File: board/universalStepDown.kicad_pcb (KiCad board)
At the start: 4 copper layers, 19.5 x 10.5 mm, 15 parts, among them J1 IO, U1 SY8105

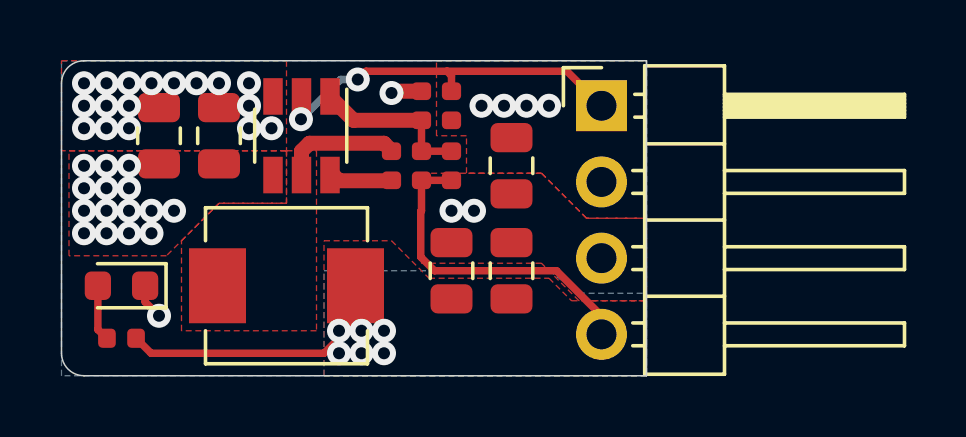
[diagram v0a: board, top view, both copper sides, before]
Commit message: Fix issues by cednik, prepare multi-voltage variant
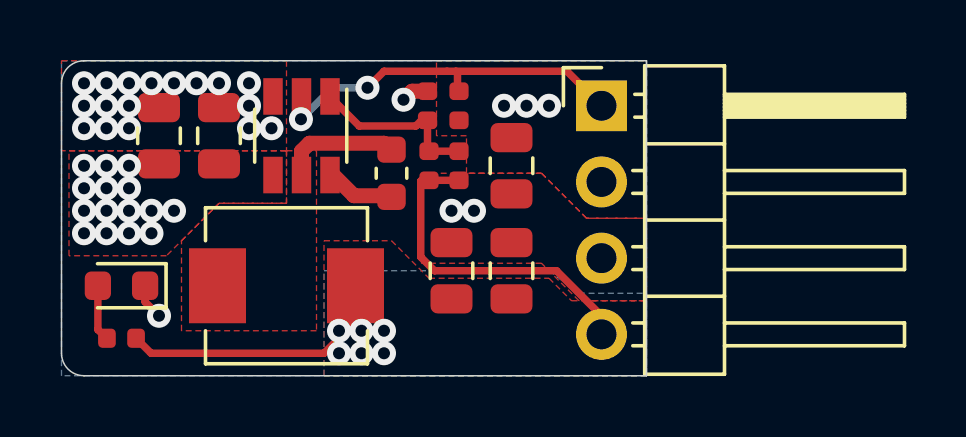
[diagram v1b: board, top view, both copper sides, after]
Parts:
- C2: footprint Capacitor_SMD:C_0402_1005Metric -> Capacitor_SMD:C_0603_1608Metric
- R2: value 27k -> 27k (for 5V)/44.2k (for 3V3)
- R3: value 47k -> 1M
- moved C2 0.25 mm to (86.0, 85.2)
- moved C3 0.25 mm to (88.2, 85.0)
- moved R1 0.25 mm to (87.2, 85.0)
- moved R3 0.25 mm to (88.2, 83.0)
- moved R2 0.20 mm to (87.2, 83.0)
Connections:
- net +5V renamed VOUT
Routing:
- net VCC: vias 19 -> 18
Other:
- board text added: "${VOLTAGE}"
- board text added: "EN VIN GND VOUT"
- board text removed: "EN VIN GND 5VOUT"

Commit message: Prepare Makefile
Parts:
- J1: footprint Connector_PinHeader_2.54mm:PinHeader_1x04_P2.54mm_Horizontal -> universalStepDown:PinHeader_1x04_P2.54mm_Horizontal
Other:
- board text added: "VOLTAGE_VARIANT"
- board text removed: "${VOLTAGE}"
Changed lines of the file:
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@@
     (add_net VOUT)
+  )
+  (module universalStepDown:PinHeader_1x04_P2.54mm_Horizontal (layer F.Cu)
+    (at 93 83)
+    (descr "Through hole angled pin header, 1x04, 2.54mm pitch, 6mm pin length, single row")
+    (tags "Through hole angled pin header THT 1x04 2.54mm single row")
+    (fp_text reference J1 (at 0 -2.5) (layer F.SilkS) hide
+      (effects (font (size 1 1) (thickness 0.15)))
+    )
+    (fp_text value IO (at 0 10.5) (layer F.Fab)
+      (effects (font (size 1 1) (thickness 0.15)))
+    )
+    (fp_line (start -0.32 -0.32) (end 1.5 -0.32) (layer F.Fab) (width 0.1))
+    (fp_line (start -0.32 -0.32) (end -0.32 0.32) (layer F.Fab) (width 0.1))
+    (fp_line (start -0.32 0.32) (end 1.5 0.32) (layer F.Fab) (width 0.1))
+    (fp_line (start -0.32 2.22) (end 1.5 2.22) (layer F.Fab) (width 0.1))
+    (fp_line (start -0.32 2.22) (end -0.32 2.86) (layer F.Fab) (width 0.1))
+    (fp_line (start -0.32 2.86) (end 1.5 2.86) (layer F.Fab) (width 0.1))
+    (fp_line (start -0.32 4.76) (end 1.5 4.76) (layer F.Fab) (width 0.1))
+    (fp_line (start -0.32 4.76) (end -0.32 5.4) (layer F.Fab) (width 0.1))
+    (fp_line (start -0.32 5.4) (end 1.5 5.4) (layer F.Fab) (width 0.1))
+    (fp_line (start -0.32 7.3) (end 1.5 7.3) (layer F.Fab) (width 0.1))
+    (fp_line (start -0.32 7.3) (end -0.32 7.94) (layer F.Fab) (width 0.1))
+    (fp_line (start -0.32 7.94) (end 1.5 7.94) (layer F.Fab) (width 0.1))
+    (fp_line (start 1.11 -0.38) (end 1.44 -0.38) (layer F.SilkS) (width 0.12))
+    (fp_line (start 1.11 0.38) (end 1.44 0.38) (layer F.SilkS) (width 0.12))
+    (fp_line (start 1.042929 2.16) (end 1.44 2.16) (layer F.SilkS) (width 0.12))
+    (fp_line (start 1.042929 2.92) (end 1.44 2.92) (layer F.SilkS) (width 0.12))
+    (fp_line (start 1.042929 4.7) (end 1.44 4.7) (layer F.SilkS) (width 0.12))
+    (fp_line (start 1.042929 5.46) (end 1.44 5.46) (layer F.SilkS) (width 0.12))
+    (fp_line (start 1.042929 7.24) (end 1.44 7.24) (layer F.SilkS) (width 0.12))
+    (fp_line (start 1.042929 8) (end 1.44 8) (layer F.SilkS) (width 0.12))
+    (fp_line (start -1.8 -1.8) (end -1.8 9.4) (layer F.CrtYd) (width 0.05))
+    (fp_line (start -1.8 9.4) (end 1 9.4) (layer F.CrtYd) (width 0.05))
+    (fp_line (start 1 9.4) (end 1 -1.8) (layer F.CrtYd) (width 0.05))
+    (fp_line (start 1 -1.8) (end -1.8 -1.8) (layer F.CrtYd) (width 0.05))
+    (pad 1 thru_hole rect (at 0 0) (size 1.7 1.7) (drill 1) (layers *.Cu *.Mask)
+      (net 6 ENABLE))
+    (pad 2 thru_hole oval (at 0 2.54) (size 1.7 1.7) (drill 1) (layers *.Cu *.Mask)
+      (net 3 VCC))
+    (pad 3 thru_hole oval (at 0 5.08) (size 1.7 1.7) (drill 1) (layers *.Cu *.Mask)
+      (net 1 GND))
+    (pad 4 thru_hole oval (at 0 7.62) (size 1.7 1.7) (drill 1) (layers *.Cu *.Mask)
+      (net 8 VOUT))
+    (model ${KISYS3DMOD}/Connector_PinHeader_2.54mm.3dshapes/PinHeader_1x04_P2.54mm_Horizontal.wrl
+      (at (xyz 0 0 0))
+      (scale (xyz 1 1 1))
+      (rotate (xyz 0 0 0))
+    )
   )
   (module Capacitor_SMD:C_0603_1608Metric (layer F.Cu)
@@
       (net 2 "Net-(C2-Pad1)"))
   )
-  (module Connector_PinHeader_2.54mm:PinHeader_1x04_P2.54mm_Horizontal (layer F.Cu)
-    (at 93 83)
-    (descr "Through hole angled pin header, 1x04, 2.54mm pitch, 6mm pin length, single row")
-    (tags "Through hole angled pin header THT 1x04 2.54mm single row")
-    (fp_text reference J1 (at 4.385 -2.27) (layer F.SilkS) hide
-      (effects (font (size 1 1) (thickness 0.15)))
-    )
-    (fp_text value IO (at 4.385 9.89) (layer F.Fab)
-      (effects (font (size 1 1) (thickness 0.15)))
-    )
-    (fp_line (start 2.135 -1.27) (end 4.04 -1.27) (layer F.Fab) (width 0.1))
-    (fp_line (start 4.04 -1.27) (end 4.04 8.89) (layer F.Fab) (width 0.1))
-    (fp_line (start 4.04 8.89) (end 1.5 8.89) (layer F.Fab) (width 0.1))
-    (fp_line (start 1.5 8.89) (end 1.5 -0.635) (layer F.Fab) (width 0.1))
-    (fp_line (start 1.5 -0.635) (end 2.135 -1.27) (layer F.Fab) (width 0.1))
-    (fp_line (start -0.32 -0.32) (end 1.5 -0.32) (layer F.Fab) (width 0.1))
-    (fp_line (start -0.32 -0.32) (end -0.32 0.32) (layer F.Fab) (width 0.1))
-    (fp_line (start -0.32 0.32) (end 1.5 0.32) (layer F.Fab) (width 0.1))
-    (fp_line (start 4.04 -0.32) (end 10.04 -0.32) (layer F.Fab) (width 0.1))
-    (fp_line (start 10.04 -0.32) (end 10.04 0.32) (layer F.Fab) (width 0.1))
-    (fp_line (start 4.04 0.32) (end 10.04 0.32) (layer F.Fab) (width 0.1))
-    (fp_line (start -0.32 2.22) (end 1.5 2.22) (layer F.Fab) (width 0.1))
-    (fp_line (start -0.32 2.22) (end -0.32 2.86) (layer F.Fab) (width 0.1))
-    (fp_line (start -0.32 2.86) (end 1.5 2.86) (layer F.Fab) (width 0.1))
-    (fp_line (start 4.04 2.22) (end 10.04 2.22) (layer F.Fab) (width 0.1))
-    (fp_line (start 10.04 2.22) (end 10.04 2.86) (layer F.Fab) (width 0.1))
-    (fp_line (start 4.04 2.86) (end 10.04 2.86) (layer F.Fab) (width 0.1))
-    (fp_line (start -0.32 4.76) (end 1.5 4.76) (layer F.Fab) (width 0.1))
-    (fp_line (start -0.32 4.76) (end -0.32 5.4) (layer F.Fab) (width 0.1))
-    (fp_line (start -0.32 5.4) (end 1.5 5.4) (layer F.Fab) (width 0.1))
-    (fp_line (start 4.04 4.76) (end 10.04 4.76) (layer F.Fab) (width 0.1))
-    (fp_line (start 10.04 4.76) (end 10.04 5.4) (layer F.Fab) (width 0.1))
-    (fp_line (start 4.04 5.4) (end 10.04 5.4) (layer F.Fab) (width 0.1))
-    (fp_line (start -0.32 7.3) (end 1.5 7.3) (layer F.Fab) (width 0.1))
-    (fp_line (start -0.32 7.3) (end -0.32 7.94) (layer F.Fab) (width 0.1))
-    (fp_line (start -0.32 7.94) (end 1.5 7.94) (layer F.Fab) (width 0.1))
-    (fp_line (start 4.04 7.3) (end 10.04 7.3) (layer F.Fab) (width 0.1))
-    (fp_line (start 10.04 7.3) (end 10.04 7.94) (layer F.Fab) (width 0.1))
-    (fp_line (start 4.04 7.94) (end 10.04 7.94) (layer F.Fab) (width 0.1))
-    (fp_line (start 1.44 -1.33) (end 1.44 8.95) (layer F.SilkS) (width 0.12))
-    (fp_line (start 1.44 8.95) (end 4.1 8.95) (layer F.SilkS) (width 0.12))
-    (fp_line (start 4.1 8.95) (end 4.1 -1.33) (layer F.SilkS) (width 0.12))
-    (fp_line (start 4.1 -1.33) (end 1.44 -1.33) (layer F.SilkS) (width 0.12))
-    (fp_line (start 4.1 -0.38) (end 10.1 -0.38) (layer F.SilkS) (width 0.12))
-    (fp_line (start 10.1 -0.38) (end 10.1 0.38) (layer F.SilkS) (width 0.12))
-    (fp_line (start 10.1 0.38) (end 4.1 0.38) (layer F.SilkS) (width 0.12))
-    (fp_line (start 4.1 -0.32) (end 10.1 -0.32) (layer F.SilkS) (width 0.12))
-    (fp_line (start 4.1 -0.2) (end 10.1 -0.2) (layer F.SilkS) (width 0.12))
-    (fp_line (start 4.1 -0.08) (end 10.1 -0.08) (layer F.SilkS) (width 0.12))
-    (fp_line (start 4.1 0.04) (end 10.1 0.04) (layer F.SilkS) (width 0.12))
-    (fp_line (start 4.1 0.16) (end 10.1 0.16) (layer F.SilkS) (width 0.12))
-    (fp_line (start 4.1 0.28) (end 10.1 0.28) (layer F.SilkS) (width 0.12))
-    (fp_line (start 1.11 -0.38) (end 1.44 -0.38) (layer F.SilkS) (width 0.12))
-    (fp_line (start 1.11 0.38) (end 1.44 0.38) (layer F.SilkS) (width 0.12))
-    (fp_line (start 1.44 1.27) (end 4.1 1.27) (layer F.SilkS) (width 0.12))
-    (fp_line (start 4.1 2.16) (end 10.1 2.16) (layer F.SilkS) (width 0.12))
-    (fp_line (start 10.1 2.16) (end 10.1 2.92) (layer F.SilkS) (width 0.12))
-    (fp_line (start 10.1 2.92) (end 4.1 2.92) (layer F.SilkS) (width 0.12))
-    (fp_line (start 1.042929 2.16) (end 1.44 2.16) (layer F.SilkS) (width 0.12))
-    (fp_line (start 1.042929 2.92) (end 1.44 2.92) (layer F.SilkS) (width 0.12))
-    (fp_line (start 1.44 3.81) (end 4.1 3.81) (layer F.SilkS) (width 0.12))
-    (fp_line (start 4.1 4.7) (end 10.1 4.7) (layer F.SilkS) (width 0.12))
-    (fp_line (start 10.1 4.7) (end 10.1 5.46) (layer F.SilkS) (width 0.12))
-    (fp_line (start 10.1 5.46) (end 4.1 5.46) (layer F.SilkS) (width 0.12))
-    (fp_line (start 1.042929 4.7) (end 1.44 4.7) (layer F.SilkS) (width 0.12))
-    (fp_line (start 1.042929 5.46) (end 1.44 5.46) (layer F.SilkS) (width 0.12))
-    (fp_line (start 1.44 6.35) (end 4.1 6.35) (layer F.SilkS) (width 0.12))
-    (fp_line (start 4.1 7.24) (end 10.1 7.24) (layer F.SilkS) (width 0.12))
-    (fp_line (start 10.1 7.24) (end 10.1 8) (layer F.SilkS) (width 0.12))
-    (fp_line (start 10.1 8) (end 4.1 8) (layer F.SilkS) (width 0.12))
-    (fp_line (start 1.042929 7.24) (end 1.44 7.24) (layer F.SilkS) (width 0.12))
-    (fp_line (start 1.042929 8) (end 1.44 8) (layer F.SilkS) (width 0.12))
-    (fp_line (start -1.27 0) (end -1.27 -1.27) (layer F.SilkS) (width 0.12))
-    (fp_line (start -1.27 -1.27) (end 0 -1.27) (layer F.SilkS) (width 0.12))
-    (fp_line (start -1.8 -1.8) (end -1.8 9.4) (layer F.CrtYd) (width 0.05))
-    (fp_line (start -1.8 9.4) (end 10.55 9.4) (layer F.CrtYd) (width 0.05))
-    (fp_line (start 10.55 9.4) (end 10.55 -1.8) (layer F.CrtYd) (width 0.05))
-    (fp_line (start 10.55 -1.8) (end -1.8 -1.8) (layer F.CrtYd) (width 0.05))
-    (fp_text user %R (at 2.77 3.81 90) (layer F.Fab)
-      (effects (font (size 1 1) (thickness 0.15)))
-    )
-    (pad 4 thru_hole oval (at 0 7.62) (size 1.7 1.7) (drill 1) (layers *.Cu *.Mask)
-      (net 8 VOUT))
-    (pad 3 thru_hole oval (at 0 5.08) (size 1.7 1.7) (drill 1) (layers *.Cu *.Mask)
-      (net 1 GND))
-    (pad 2 thru_hole oval (at 0 2.54) (size 1.7 1.7) (drill 1) (layers *.Cu *.Mask)
-      (net 3 VCC))
-    (pad 1 thru_hole rect (at 0 0) (size 1.7 1.7) (drill 1) (layers *.Cu *.Mask)
-      (net 6 ENABLE))
-    (model ${KISYS3DMOD}/Connector_PinHeader_2.54mm.3dshapes/PinHeader_1x04_P2.54mm_Horizontal.wrl
-      (at (xyz 0 0 0))
-      (scale (xyz 1 1 1))
-      (rotate (xyz 0 0 0))
-    )
-  )
   (module LED_SMD:LED_0603_1608Metric (layer F.Cu)
     (at 77 89 180)
@@
     )
   )
-  (gr_text ${VOLTAGE} (at 82.5 86.75 90) (layer B.SilkS)
+  (gr_text VOLTAGE_VARIANT (at 82.5 86.75 90) (layer B.SilkS)
     (effects (font (size 1.2 1.2) (thickness 0.2)) (justify mirror))
   )

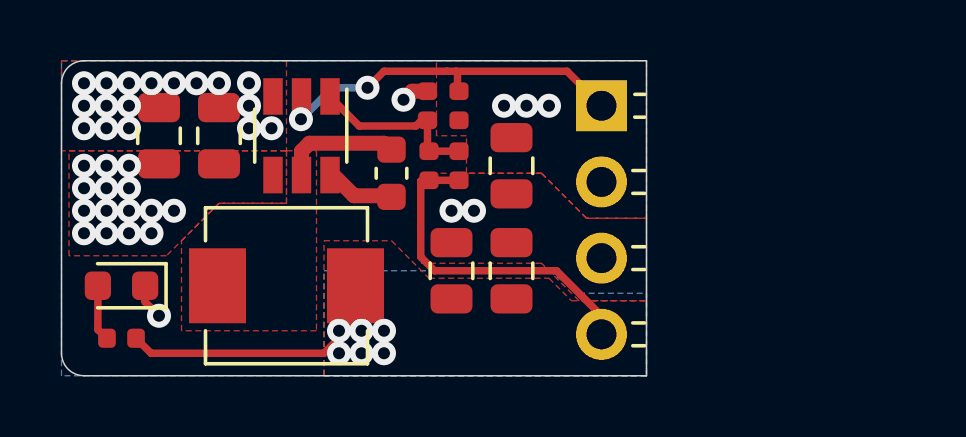
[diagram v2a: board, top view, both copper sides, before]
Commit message: Improve thermal design
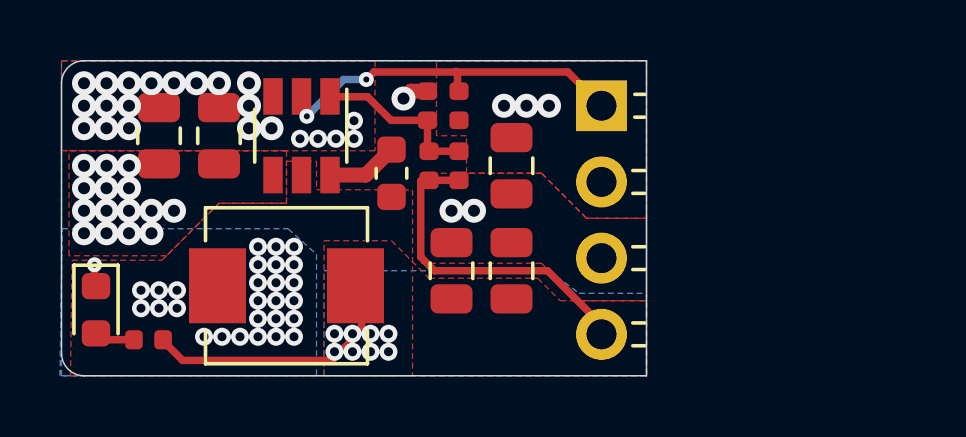
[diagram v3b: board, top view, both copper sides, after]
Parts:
- moved D1 1.17 mm to (76.2, 89.8), turned to 270 degrees
- moved R4 0.90 mm to (77.9, 90.8)
- turned C2 to 90 degrees
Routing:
- net Net-(C2-Pad1): track 4.01 -> 0.00 mm, vias 0 -> 27
- net Net-(D1-Pad2): track 1.87 -> 1.30 mm
- net VOUT: track 20.4 -> 19.8 mm, vias 6 -> 8
- net GND: track 1.91 -> 1.80 mm, vias 21 -> 26
- added copper zone on B.Cu, net Net-(C2-Pad1)
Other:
- rule via_min_drill: 0.3 -> 0.2
- rule via_min_size: 0.2 -> 0.45
- board text added: "GH: RoboticsBrno Jan Mrázek v0.2 11/2020"
- board text removed: "GH: RoboticsBrno Jan Mrázek v0.1 9/2020"
